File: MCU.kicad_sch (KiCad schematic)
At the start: 32 parts, among them IC3 TCAN330DCNT, J1 SM04B-GHS-TB, J2 Conn_01x04_Pin, J3 USB_C_Receptacle_USB2.0_16P, J4 Conn_01x04_Pin, SW1 SW_SPDT, U2 STM32G431CBU6, U3 ME6211C33M5, Y1 ECS-80-20-5PX-TR

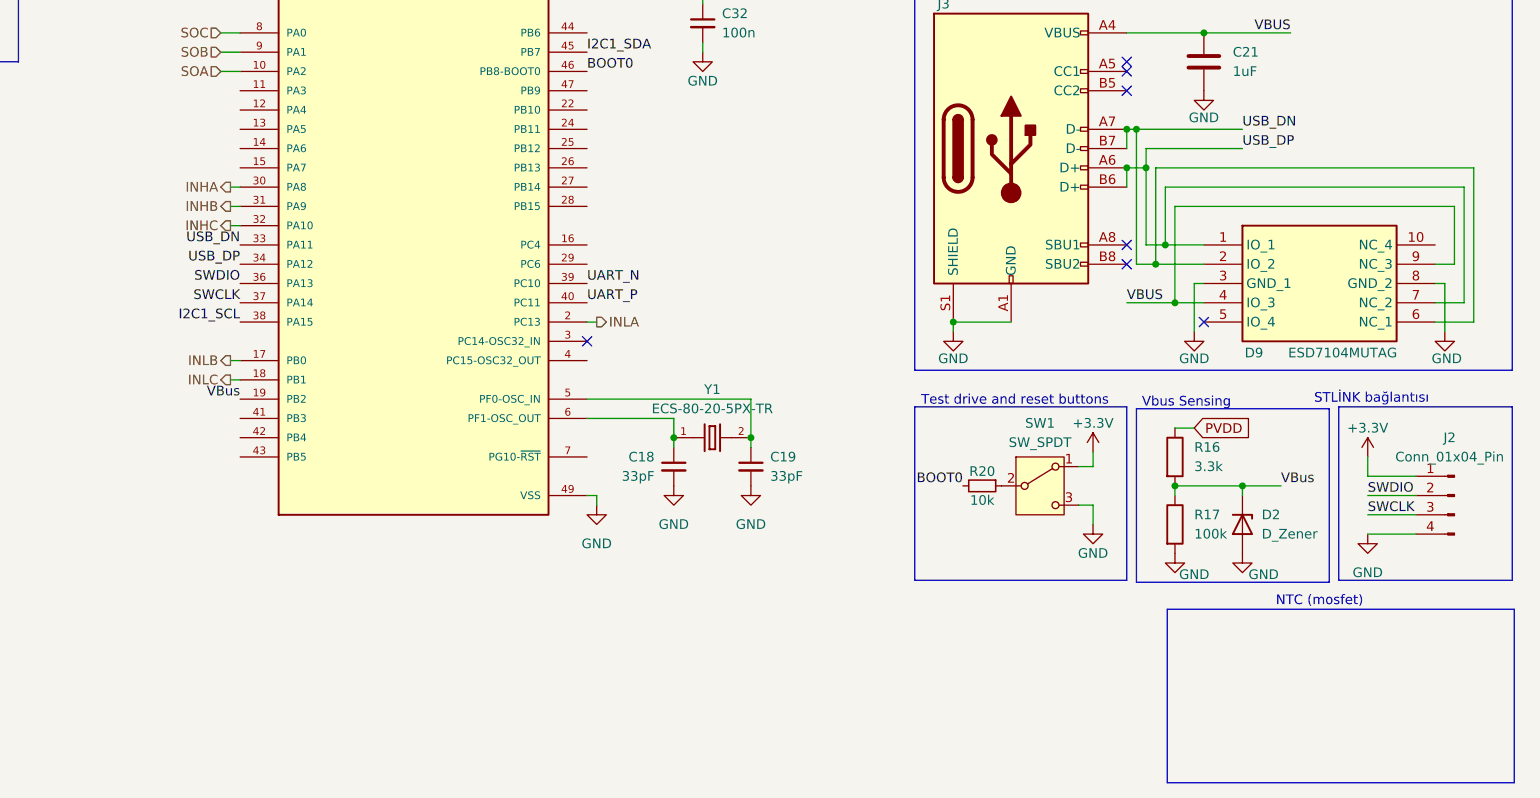
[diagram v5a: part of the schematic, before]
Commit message: added ntc sensor
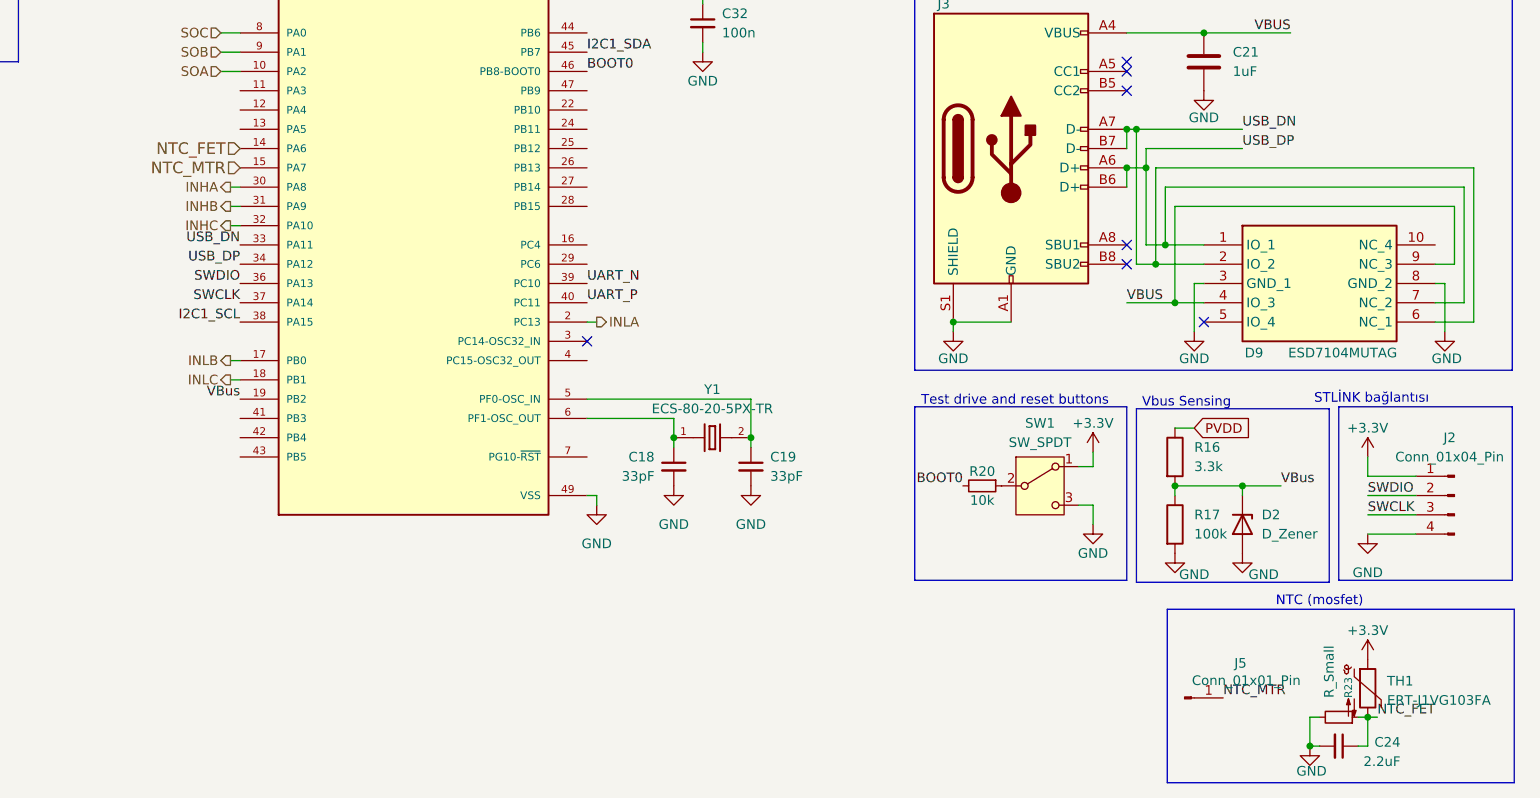
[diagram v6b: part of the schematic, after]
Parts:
- added C24: 2.2uF, Capacitor_SMD:C_0603_1608Metric, symbol Device:C_Small
- added J5: Conn_01x01_Pin, Connector_PinHeader_1.00mm:PinHeader_1x01_P1.00mm_Vertical, symbol Connector:Conn_01x01_Pin
- added R23: R_Small, Resistor_SMD:R_0603_1608Metric, symbol Device:R_Small
- added TH1: ERT-J1VG103FA, Resistor_SMD:R_0603_1608Metric, symbol Device:Thermistor_NTC
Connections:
- net +3.3V: now also TH1.1
- net GND: now also C24.2, R23.2
- net NTC_FET: now reaches U2.14 (PA6)
- net NTC_FET: now also C24.1, R23.1, TH1.2
- net NTC_MTR: now reaches U2.15 (PA7)
- net NTC_MTR: now also J5.1 (Pin_1)

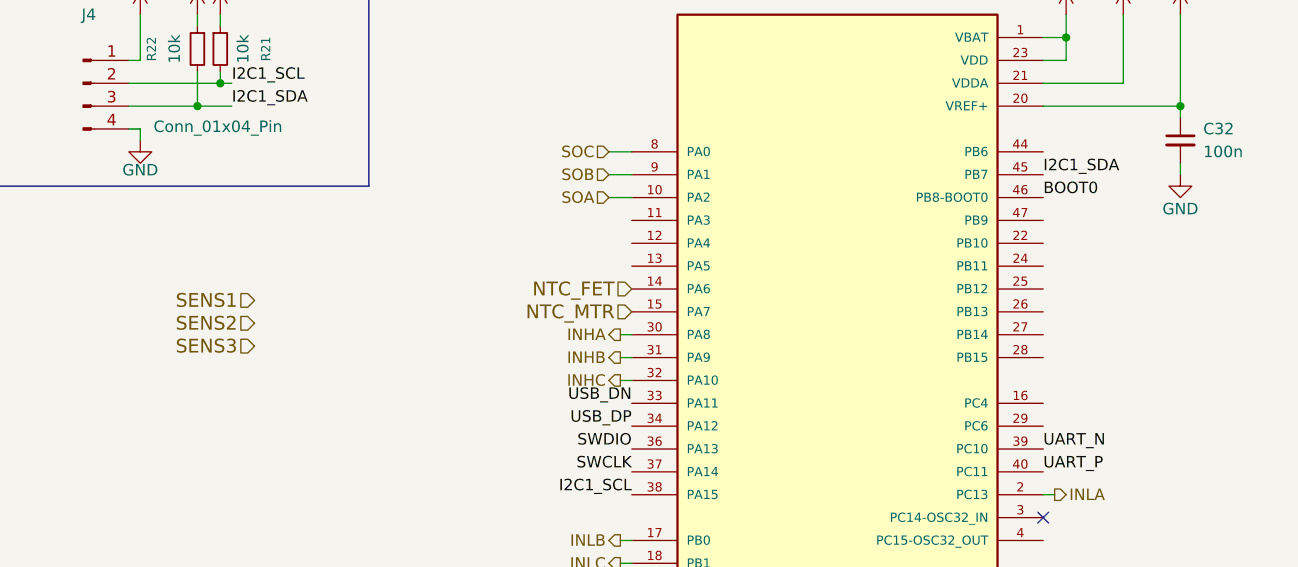
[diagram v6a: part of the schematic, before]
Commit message: vbus / current sense pins on MCU
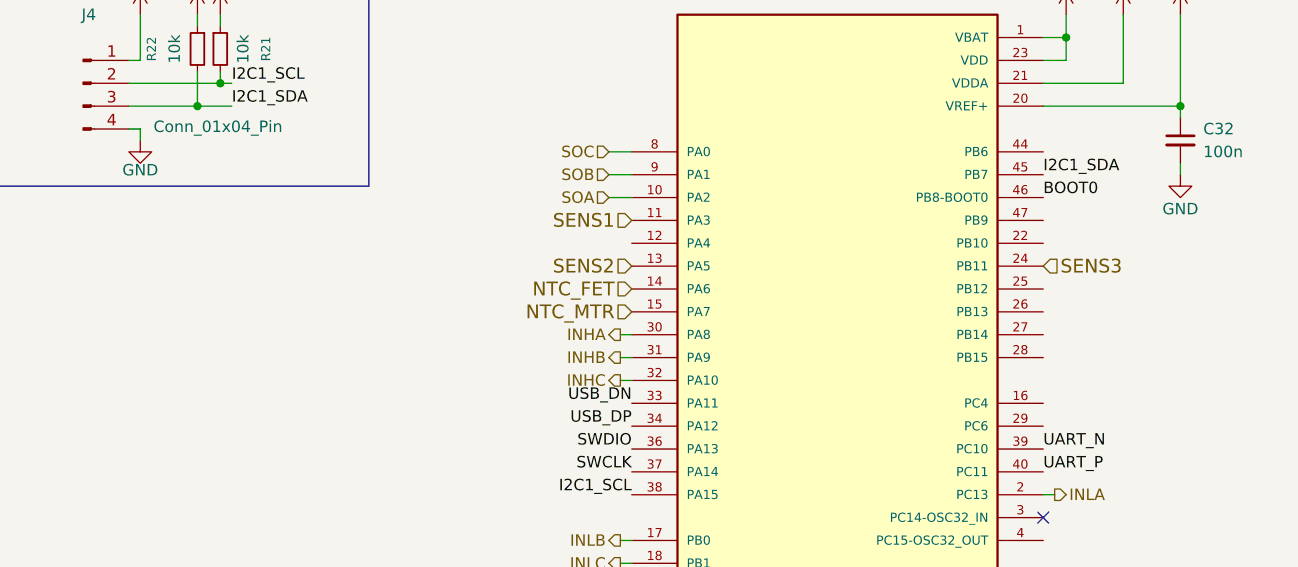
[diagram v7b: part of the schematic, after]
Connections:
- net SENS1: now also U2.11 (PA3)
- net SENS2: now also U2.13 (PA5)
- net SENS3: now also U2.24 (PB11)

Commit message: leds
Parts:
- added D3: LEDA, LED_SMD:LED_0603_1608Metric_Pad1.05x0.95mm_HandSolder, symbol Device:LED
- added D4: LEDB, LED_SMD:LED_0603_1608Metric_Pad1.05x0.95mm_HandSolder, symbol Device:LED
- added D5: LEDC, LED_SMD:LED_0603_1608Metric_Pad1.05x0.95mm_HandSolder, symbol Device:LED
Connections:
- net GND: now also D3.1 (K), D4.1 (K), D5.1 (K)
- net at U2.25 (PB12): now also D3.2 (A)
- net at U2.26 (PB13): now also D4.2 (A)
- net at U2.27 (PB14): now also D5.2 (A)
